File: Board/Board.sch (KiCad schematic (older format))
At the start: 43 parts, among them J1 5025700893, J2 Conn_01x02_Male, Q1 Q_NMOS_GSD, Q2 Q_NMOS_GSD, SW2 SW_SPST, U1 ATmega328P-AU, U2 TLV61225DCKR, U3 MCP6001UT-I_OT

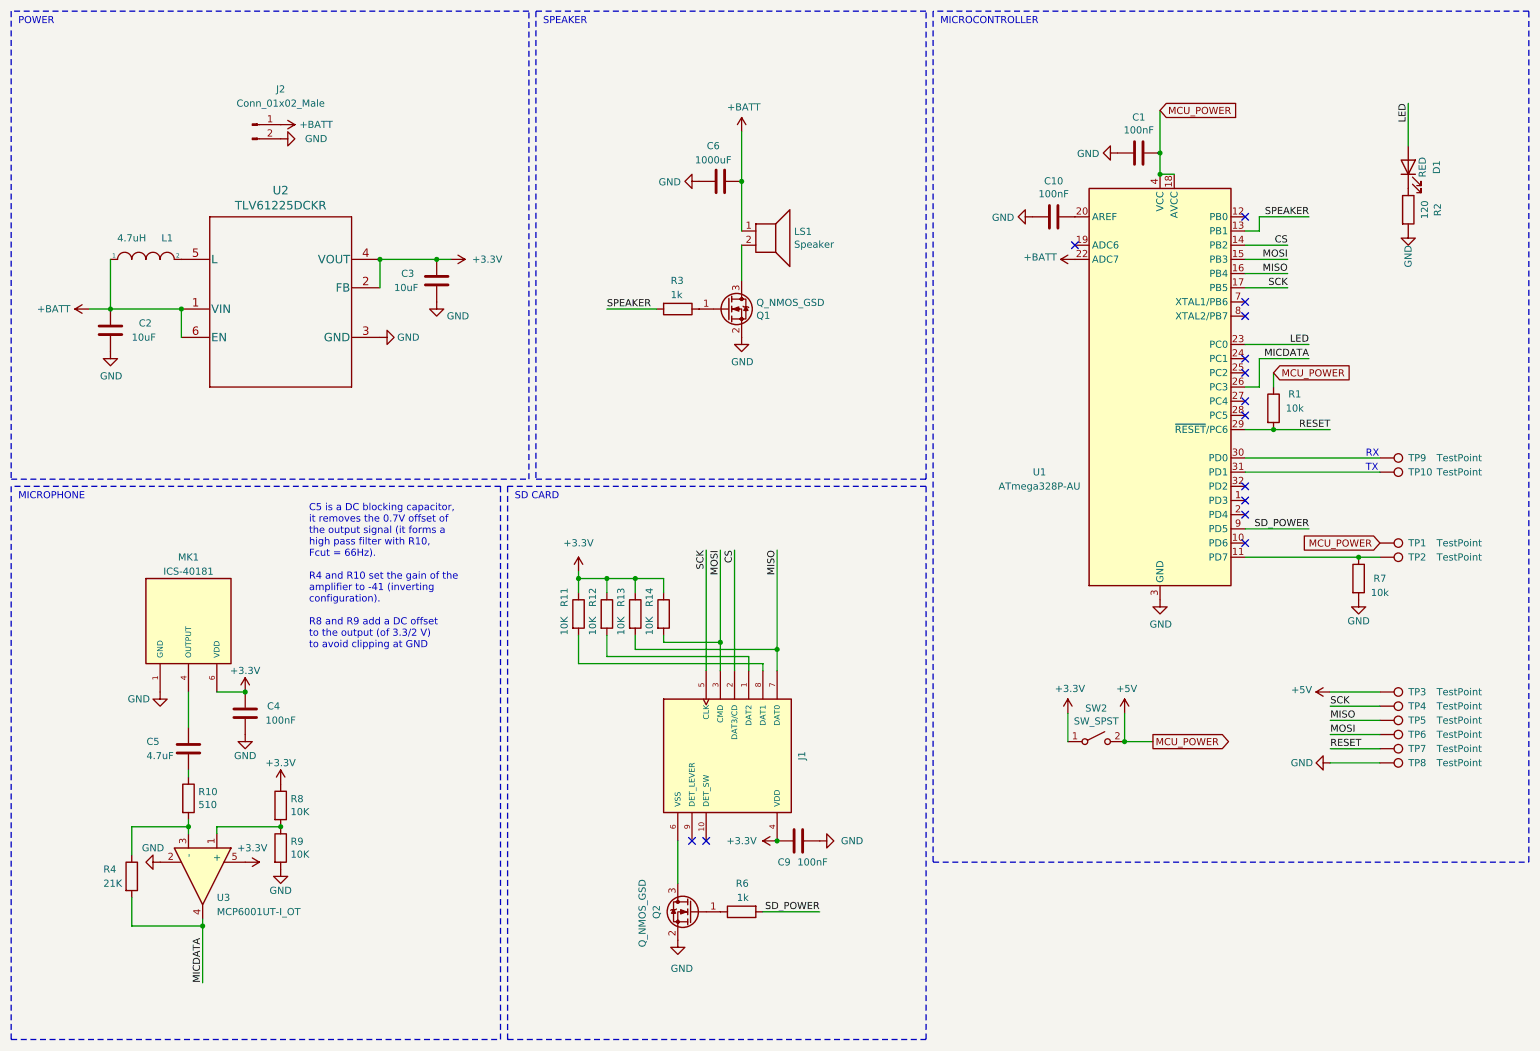
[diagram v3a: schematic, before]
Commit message: Added Gate pulldowns
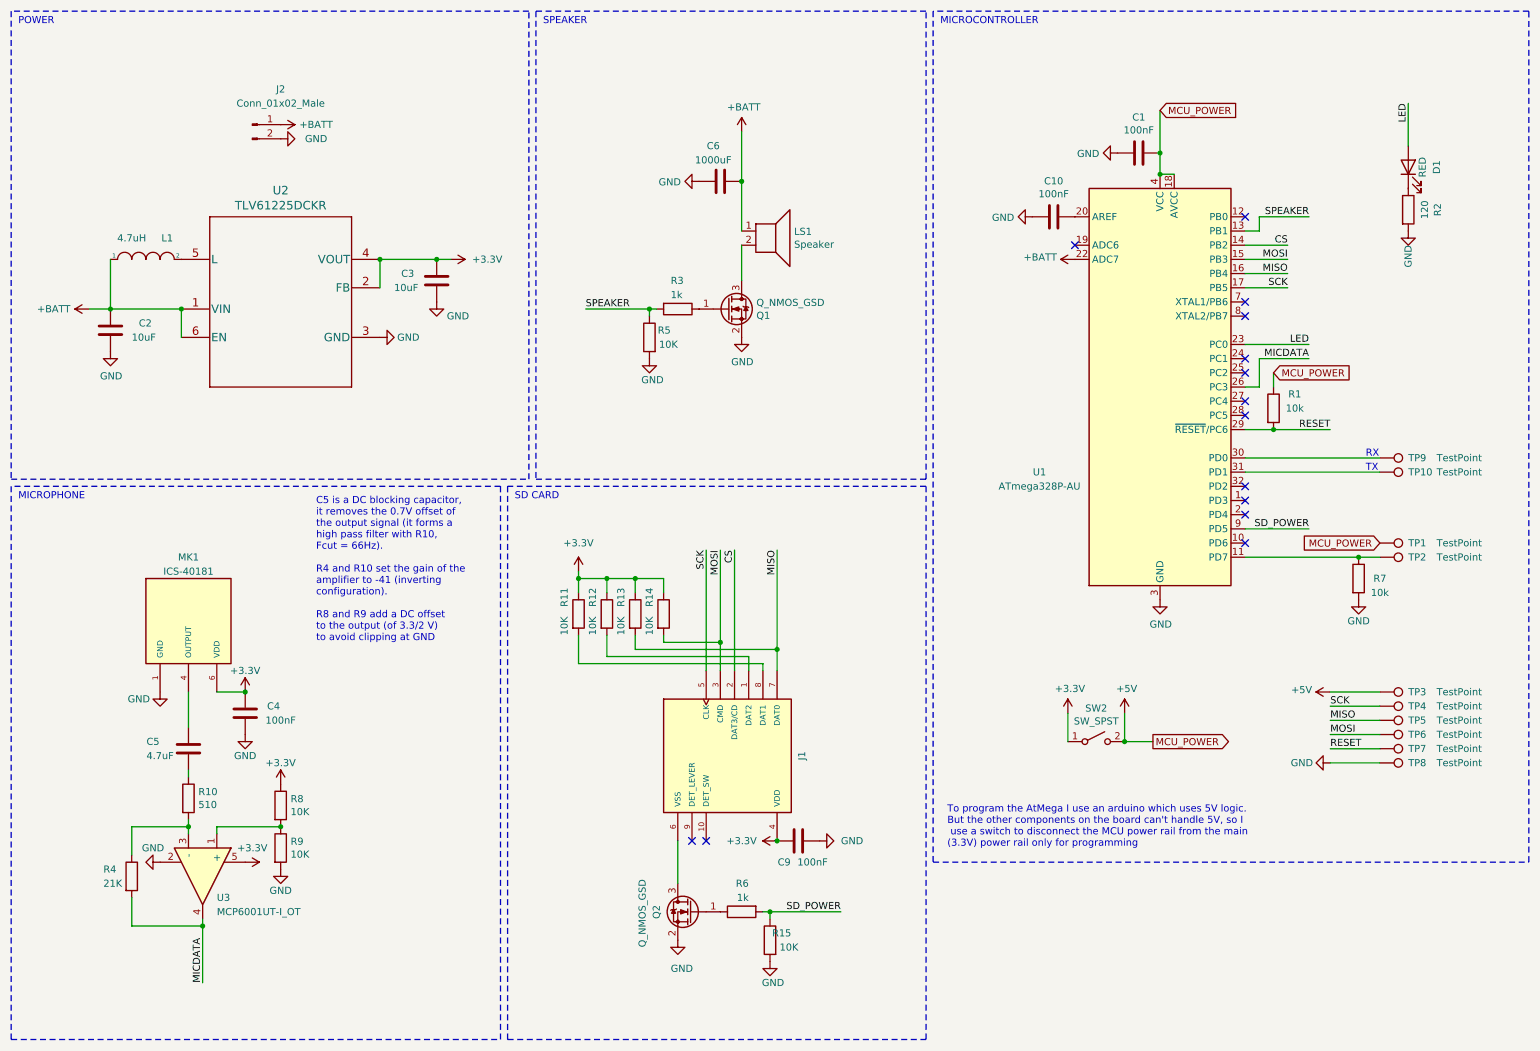
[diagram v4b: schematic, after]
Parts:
- added R15, R5: 10K, Resistor_SMD:R_0603_1608Metric, symbol Device:R
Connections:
- net GND: now also R15.2, R5.2
- net SD_POWER: now also R15.1
- net SPEAKER: now also R5.1
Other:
- note added: "To program the AtMega I use an arduino which uses 5V logic. \nBut the other components on the board can't handle 5V, so I\n use a switch to disconnect the MCU power rail from the main \n(3.3V) power rail only for programming"
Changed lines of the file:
@@
 $EndComp
 Wire Wire Line
-	5050 2600 4700 2600
-Text Label 4700 2600 0    50   ~ 0
+	5050 2600 5000 2600
+Text Label 4550 2600 0    50   ~ 0
 SPEAKER
 $Comp
@@
 $EndComp
 Wire Wire Line
-	6200 6850 5800 6850
-Text Label 6200 6850 2    50   ~ 0
+	6350 6850 5850 6850
+Text Label 6350 6850 2    50   ~ 0
 SD_POWER
 Wire Wire Line
@@
 Wire Wire Line
 	1750 6200 1750 6250
-Text Notes 2600 5000 0    50   ~ 0
+Text Notes 2650 4950 0    50   ~ 0
 C5 is a DC blocking capacitor, \nit removes the 0.7V offset of \nthe output signal (it forms a \nhigh pass filter with R10, \nFcut = 66Hz).\n\nR4 and R10 set the gain of the\namplifier to -41 (inverting \nconfiguration).\n\nR8 and R9 add a DC offset \nto the output (of 3.3/2 V)\nto avoid clipping at GND
 Wire Wire Line
@@
 LED
 NoConn ~ 9200 3850
+Wire Wire Line
+	5850 6850 5850 6900
+Connection ~ 5850 6850
+Wire Wire Line
+	5850 6850 5800 6850
+$Comp
+L power:GND #PWR020
+U 1 1 60675156
+P 5850 7200
+F 0 "#PWR020" H 5850 6950 50  0001 C CNN
+F 1 "GND" H 5950 7050 50  0000 R CNN
+F 2 "" H 5850 7200 50  0001 C CNN
+F 3 "" H 5850 7200 50  0001 C CNN
+	1    5850 7200
+	1    0    0    -1
+$EndComp
+$Comp
+L Device:R R15
+U 1 1 60672139
+P 5850 7050
+F 0 "R15" H 5700 7100 50  0000 L CNN
+F 1 "10K" H 5650 7000 50  0000 L CNN
+F 2 "Resistor_SMD:R_0603_1608Metric" V 5780 7050 50  0001 C CNN
+F 3 "~" H 5850 7050 50  0001 C CNN
+	1    5850 7050
+	-1   0    0    -1
+$EndComp
+$Comp
+L power:GND #PWR018
+U 1 1 6067AD48
+P 5000 2950
+F 0 "#PWR018" H 5000 2700 50  0001 C CNN
+F 1 "GND" H 5100 2800 50  0000 R CNN
+F 2 "" H 5000 2950 50  0001 C CNN
+F 3 "" H 5000 2950 50  0001 C CNN
+	1    5000 2950
+	1    0    0    -1
+$EndComp
+$Comp
+L Device:R R5
+U 1 1 6067AD4E
+P 5000 2800
+F 0 "R5" H 4850 2850 50  0000 L CNN
+F 1 "10K" H 4800 2750 50  0000 L CNN
+F 2 "Resistor_SMD:R_0603_1608Metric" V 4930 2800 50  0001 C CNN
+F 3 "~" H 5000 2800 50  0001 C CNN
+	1    5000 2800
+	-1   0    0    -1
+$EndComp
+Wire Wire Line
+	5000 2600 5000 2650
+Connection ~ 5000 2600
+Wire Wire Line
+	5000 2600 4550 2600
+Text Notes 7100 6400 0    50   ~ 0
+To program the AtMega I use an arduino which uses 5V logic. \nBut the other components on the board can't handle 5V, so I\n use a switch to disconnect the MCU power rail from the main \n(3.3V) power rail only for programming
 $EndSCHEMATC
